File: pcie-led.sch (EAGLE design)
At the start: 64 parts, among them IC1 LED6001, IC2 LM556D, IC3 NL27WZ07, J1 45558-0003, J2 15-24-4441, Q1 BSC340N08NS3G, Q2 BSC340N08NS3G

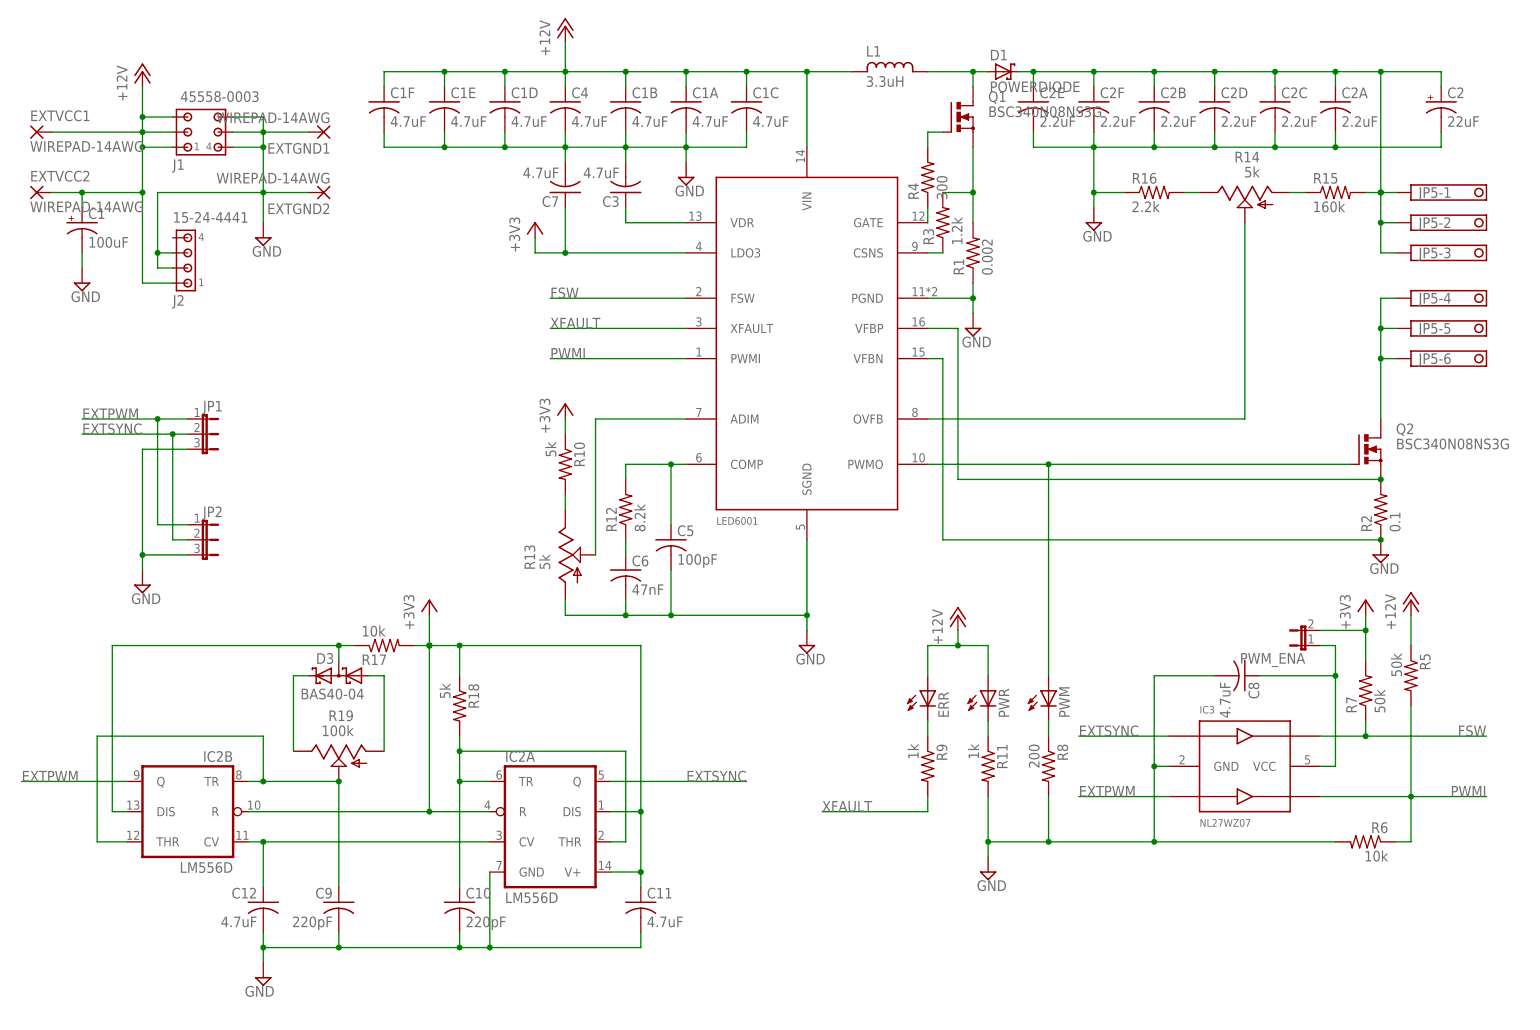
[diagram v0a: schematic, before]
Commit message: Fix errors with clock and PWM generators
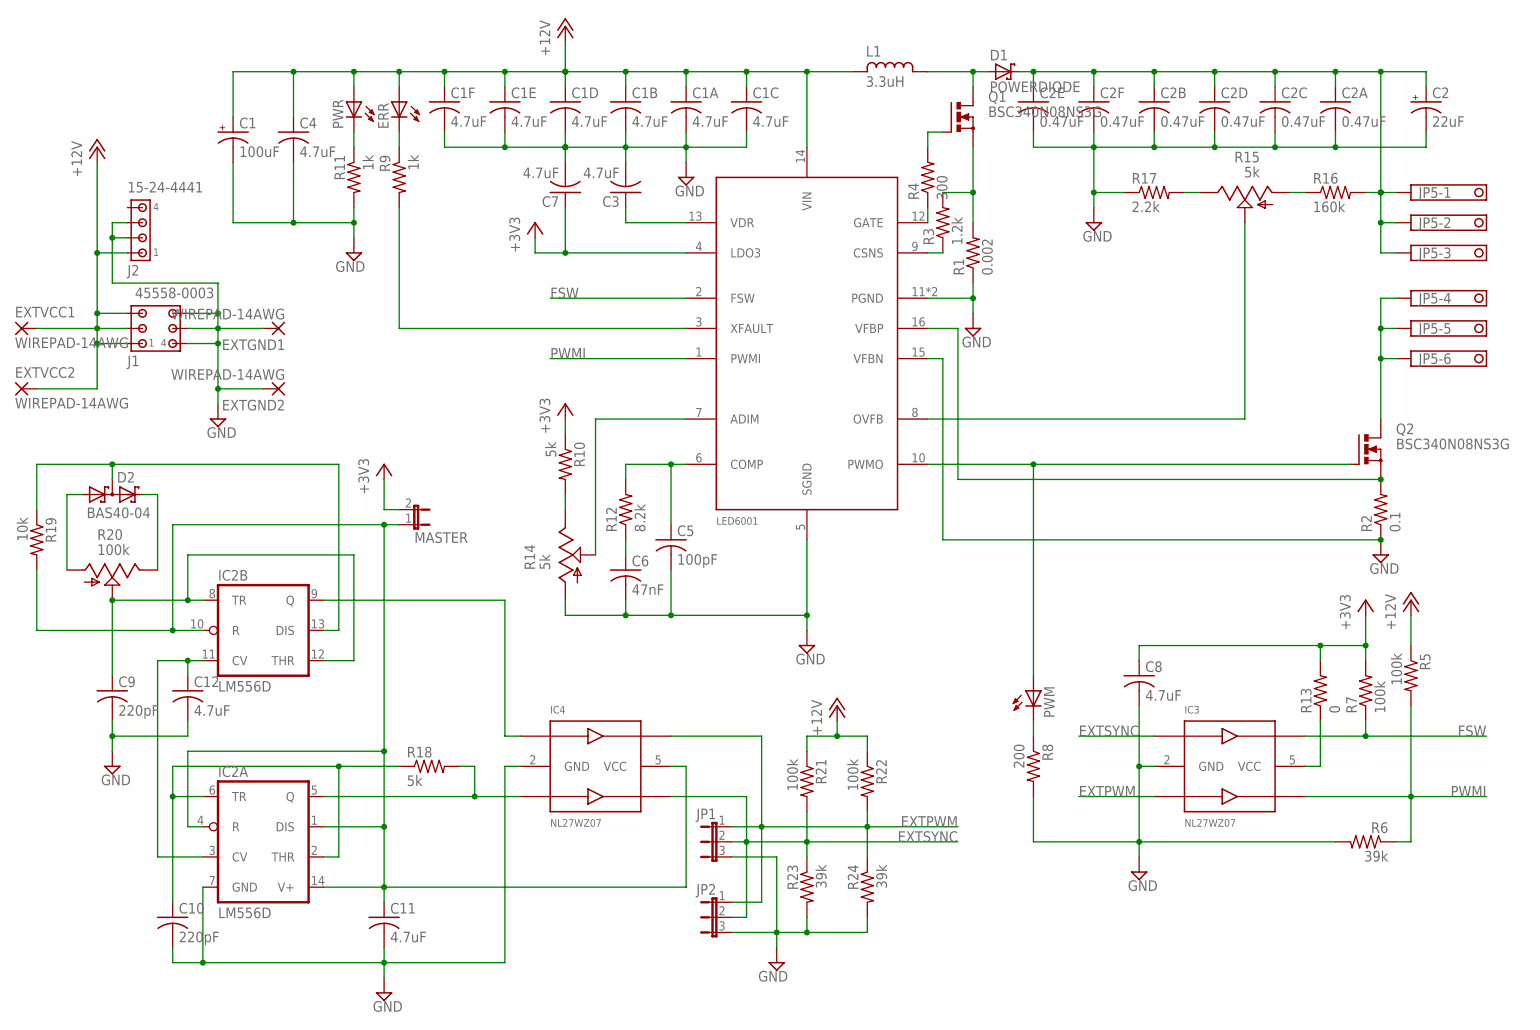
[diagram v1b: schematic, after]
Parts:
- removed D3: BAS40-04, diode:BAS40-04
- removed PWM_ENA: (no value), parts:JP1E
- added D2: BAS40-04, diode:BAS40-04
- added IC4: NL27WZ07, parts:NL27WZ07
- added MASTER: (no value), parts:JP1E
- added R20: 100k, parts:P260T
- added R21, R22: 100k, resistor:R-US_R0603
- added R23, R24: 39k, resistor:R-US_R0603
- C2A, C2B, C2C, C2D, C2E, C2F: value 2.2uF -> 0.47uF
- R13: value 5k -> 0; device parts:ST4ETB -> resistor:R-US_R0603
- R15: value 160k -> 5k; device resistor:R-US_R0603 -> parts:ST4ETB
- R16: value 2.2k -> 160k
- R17: value 10k -> 2.2k
- R19: value 100k -> 10k; device parts:P260T -> resistor:R-US_R0603
- R5, R7: value 50k -> 100k
- R6: value 10k -> 39k
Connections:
- new net N$16: IC3.VCC, R13.1
- new net N$6: IC2A.Q, IC4.IN2, R18.2
- new net N$8: IC2B.Q, IC4.IN1
- net +12V: now also R21.1, R22.1
- net +3V3: now also C8.1, MASTER.2, R13.2; no longer C11.1, IC2A.DIS, IC2A.R, IC2A.V+, IC2B.R, PWM_ENA.2, R17.2, R18.1
- net EXTPWM: now also IC4.OUT1, R22.2, R24.1; no longer IC2B.Q
- net EXTSYNC: now also IC4.OUT2, R21.2, R23.1; no longer IC2A.Q
- net GND: now also IC4.GND, R14.A, R17.1, R23.2, R24.2; no longer R13.A, R16.1
- net LED+: now also R16.2; no longer R15.2
- net N$11: now also R15.S; no longer R14.S
- net N$12: now also R14.S; no longer R13.S
- net N$13: now also R15.E, R17.2; no longer R14.E, R16.2
- net N$14: now also R14.E; no longer R13.E
- net N$21: now also R18.1; no longer R18.2
- net N$23: now also D2.C2, R20.E; no longer D3.C2, R19.E
- net N$24: now also D2.A1, R20.A; no longer D3.A1, R19.A
- net N$25: now also R20.S; no longer R19.S
- net N$26: now also D2.C1A2, R19.1; no longer D3.C1A2, R17.1
- net N$4: now also C11.1, IC2A.DIS, IC2A.R, IC2A.V+, IC2B.R, IC4.VCC, MASTER.1, R19.2; no longer C8.1, IC3.VCC, PWM_ENA.1
- net N$7: now also R15.A, R16.1; no longer R14.A, R15.1
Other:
- moved on the sheet: C1, C10, C11, C12, C1D, C1E, C1F, C2, C4, C8, C9, ERR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
